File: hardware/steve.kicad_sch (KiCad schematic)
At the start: 10 parts, among them J1 Conn_ARM_JTAG_SWD_10, U1 STM32F407VGTx, Y1 12MHz, Y2 32.768kHz

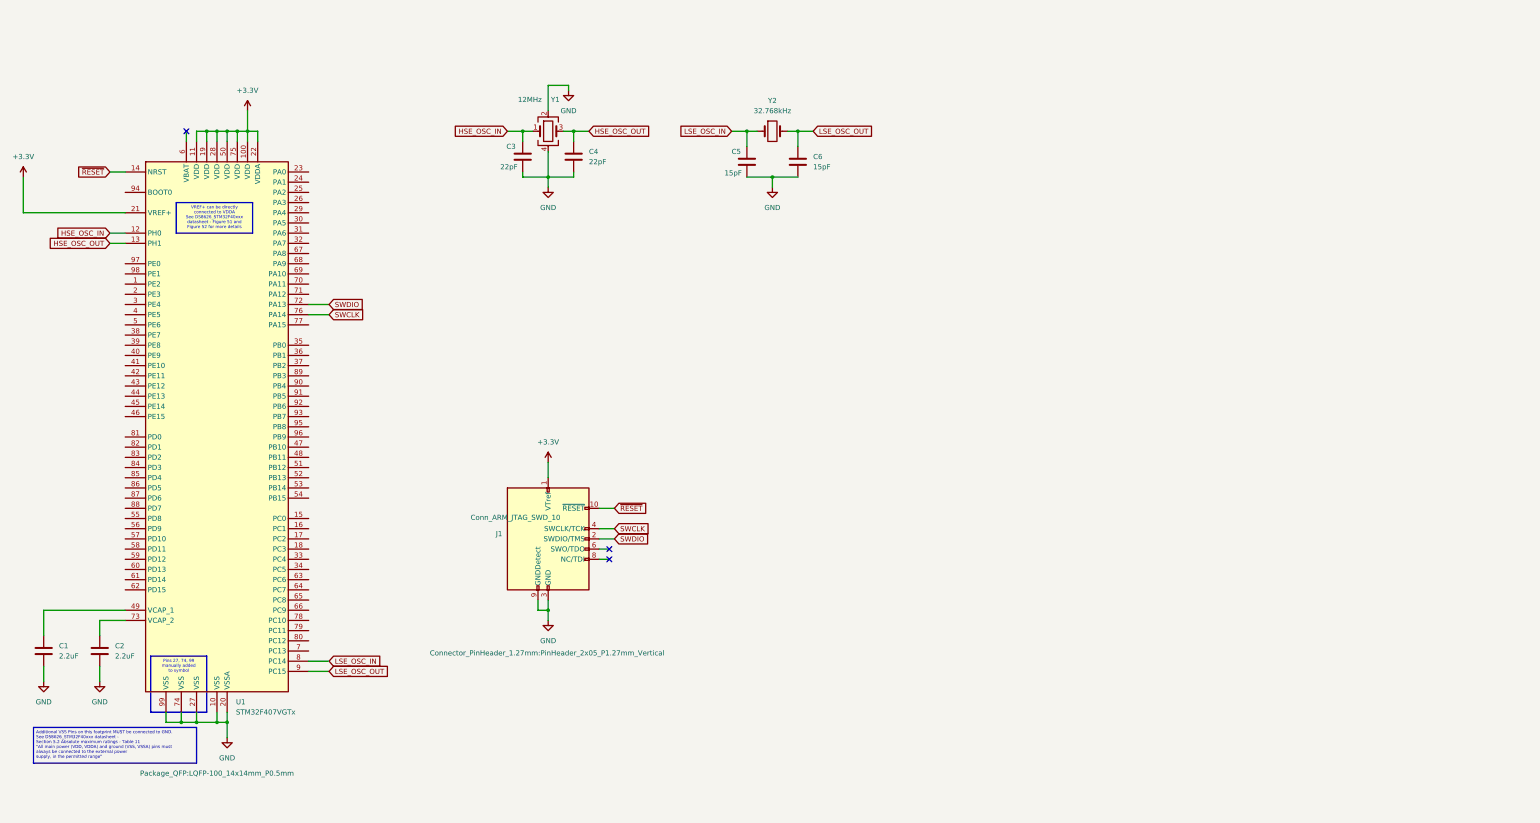
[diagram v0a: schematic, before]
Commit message: Added 5V reg and other components
Added 5V regulator circuit to schematic. Added project libraries for imported symbols and footprints. Added additional components to schematic.
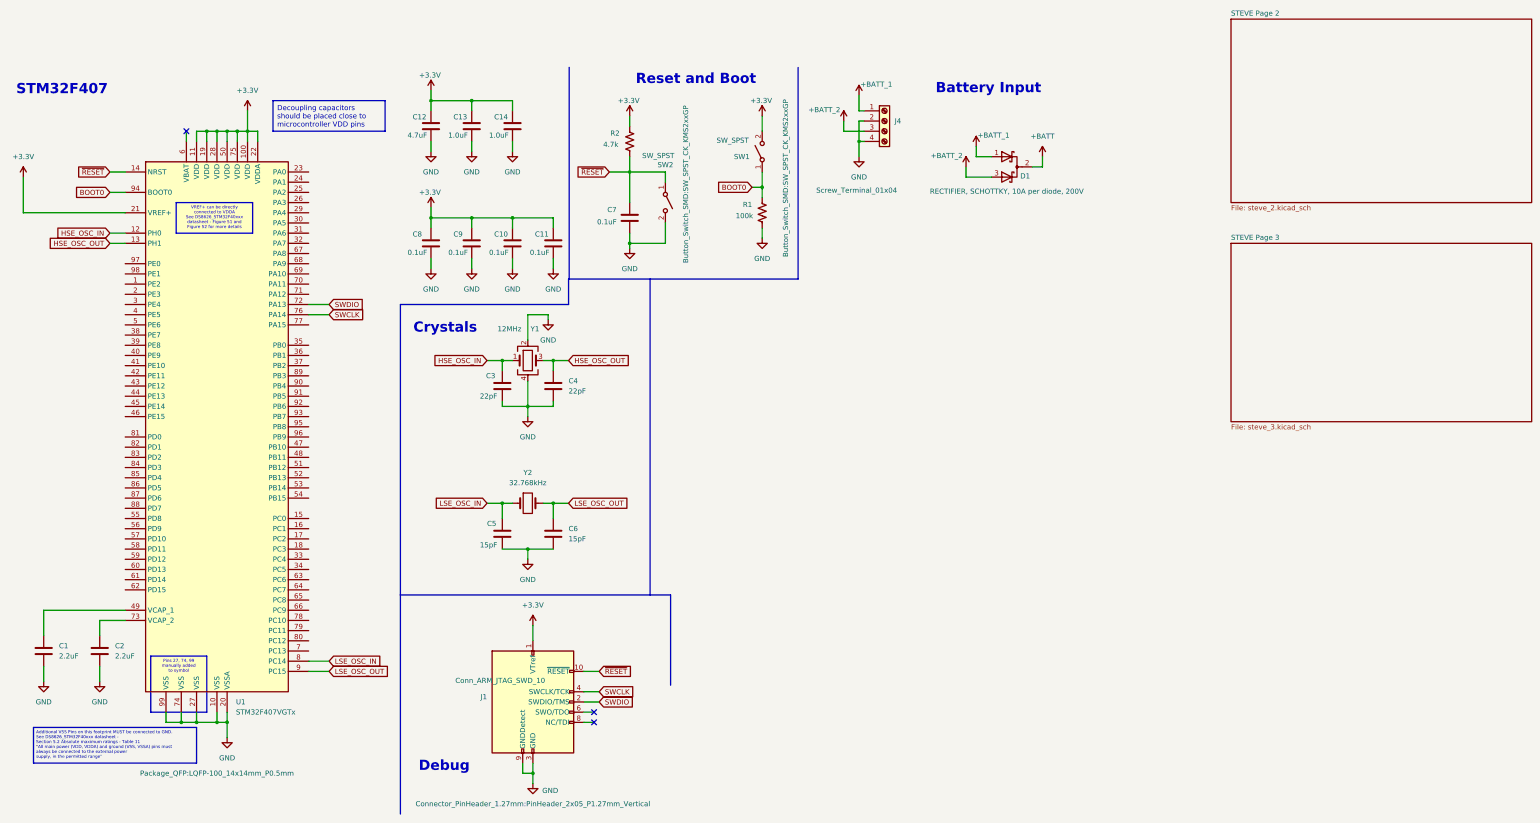
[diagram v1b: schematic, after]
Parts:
- added C10, C11, C7, C8, C9: 0.1uF, Capacitor_SMD:C_0603_1608Metric, symbol Device:C
- added C12: 4.7uF, Capacitor_SMD:C_0603_1608Metric, symbol Device:C
- added C13, C14: 1.0uF, Capacitor_SMD:C_0603_1608Metric, symbol Device:C
- added D1: RECTIFIER, SCHOTTKY, 10A per diode, 200V, Package_TO_SOT_SMD:TO-263-2, symbol Device:D_Schottky_Dual_CommonCathode_AKA_Parallel
- added J4: Screw_Terminal_01x04, TerminalBlock_Phoenix:TerminalBlock_Phoenix_PT-1,5-4-5.0-H_1x04_P5.00mm_Horizontal, symbol Connector:Screw_Terminal_01x04
- added R1: 100k, Resistor_SMD:R_0603_1608Metric, symbol Device:R_US
- added R2: 4.7k, Resistor_SMD:R_0603_1608Metric, symbol Device:R_US
- added SW1, SW2: SW_SPST, Button_Switch_SMD:SW_SPST_CK_KMS2xxGP, symbol Switch:SW_SPST
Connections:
- net +3.3V: now also C10.1, C11.1, C12.1, C13.1, C14.1, C8.1, C9.1, R2.1, SW1.2 (B)
- net GND: now also C10.2, C11.2, C12.2, C13.2, C14.2, C7.2, C8.2, C9.2, J4.2 (Pin_2), J4.4 (Pin_4), R1.2, SW2.2 (B)
- net ~{RESET}: now also C7.1, R2.2, SW2.1 (A)
- net BOOT0: now reaches U1.94 (BOOT0)
- net BOOT0: now also R1.1, SW1.1 (A)
- new net +BATT: D1.2 (K)
- new net +BATT_1: D1.1 (A), J4.1 (Pin_1)
- new net +BATT_2: D1.3 (A), J4.3 (Pin_3)
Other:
- added sheet STEVE Page 2 (steve_2.kicad_sch)
- added sheet STEVE Page 3 (steve_3.kicad_sch)
- note added: "Battery Input"
- note added: "Crystals"
- note added: "Debug"
- note added: "Reset and Boot"
- note added: "STM32F407"
- moved on the sheet: C3, C4, C5, C6, J1, Y1, Y2

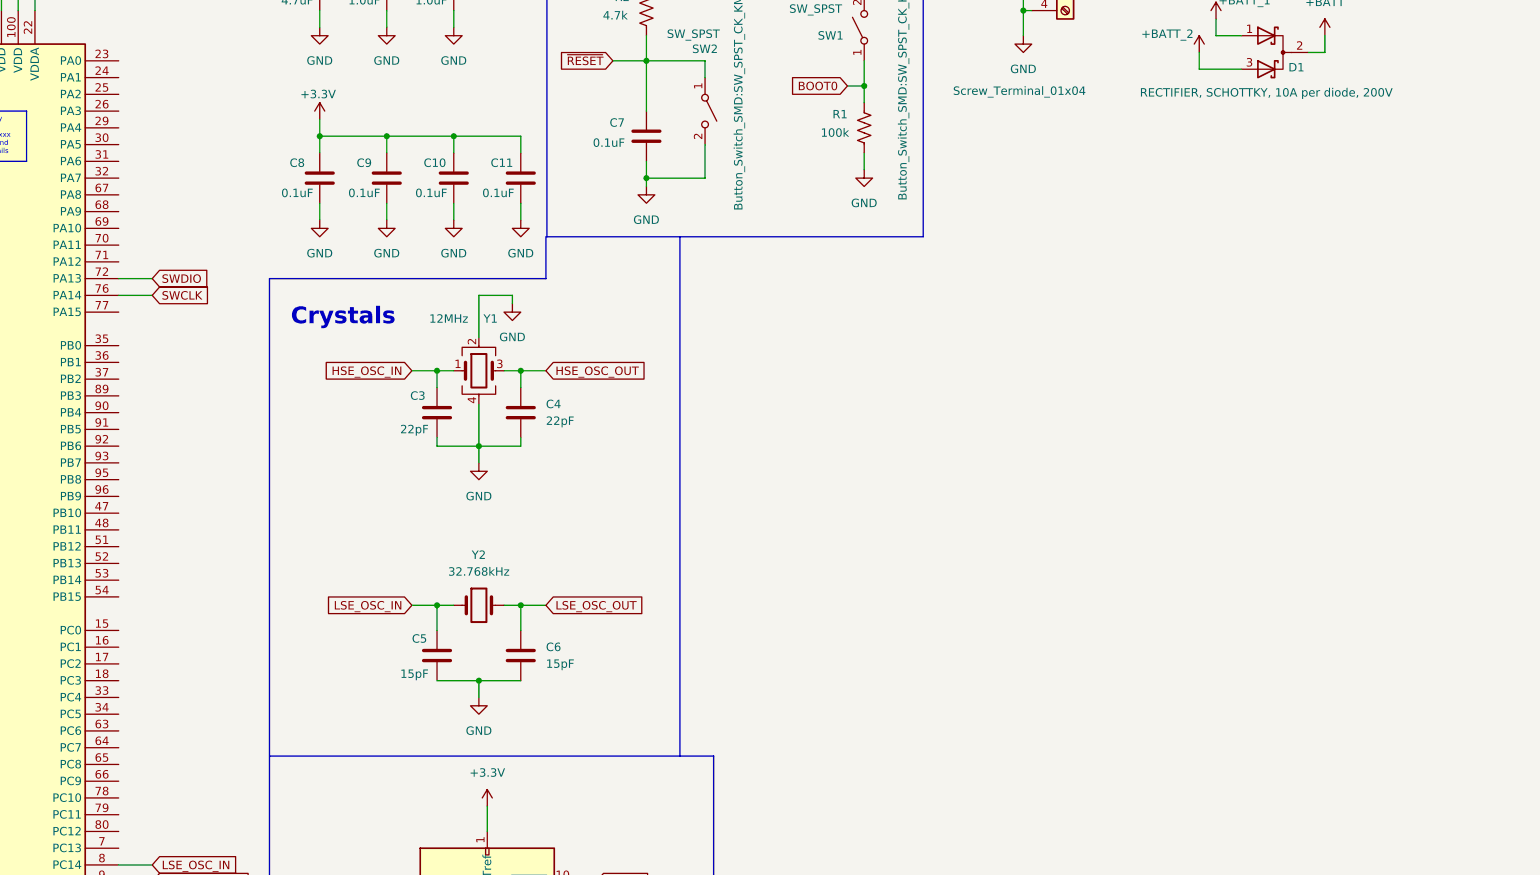
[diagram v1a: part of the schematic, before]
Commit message: import BMP388, add BMP388 to pcb and sch
Import BMP388 symbol and footprint to project imports dir. Add BMP388 symbol to schematic and footprint to pcb.
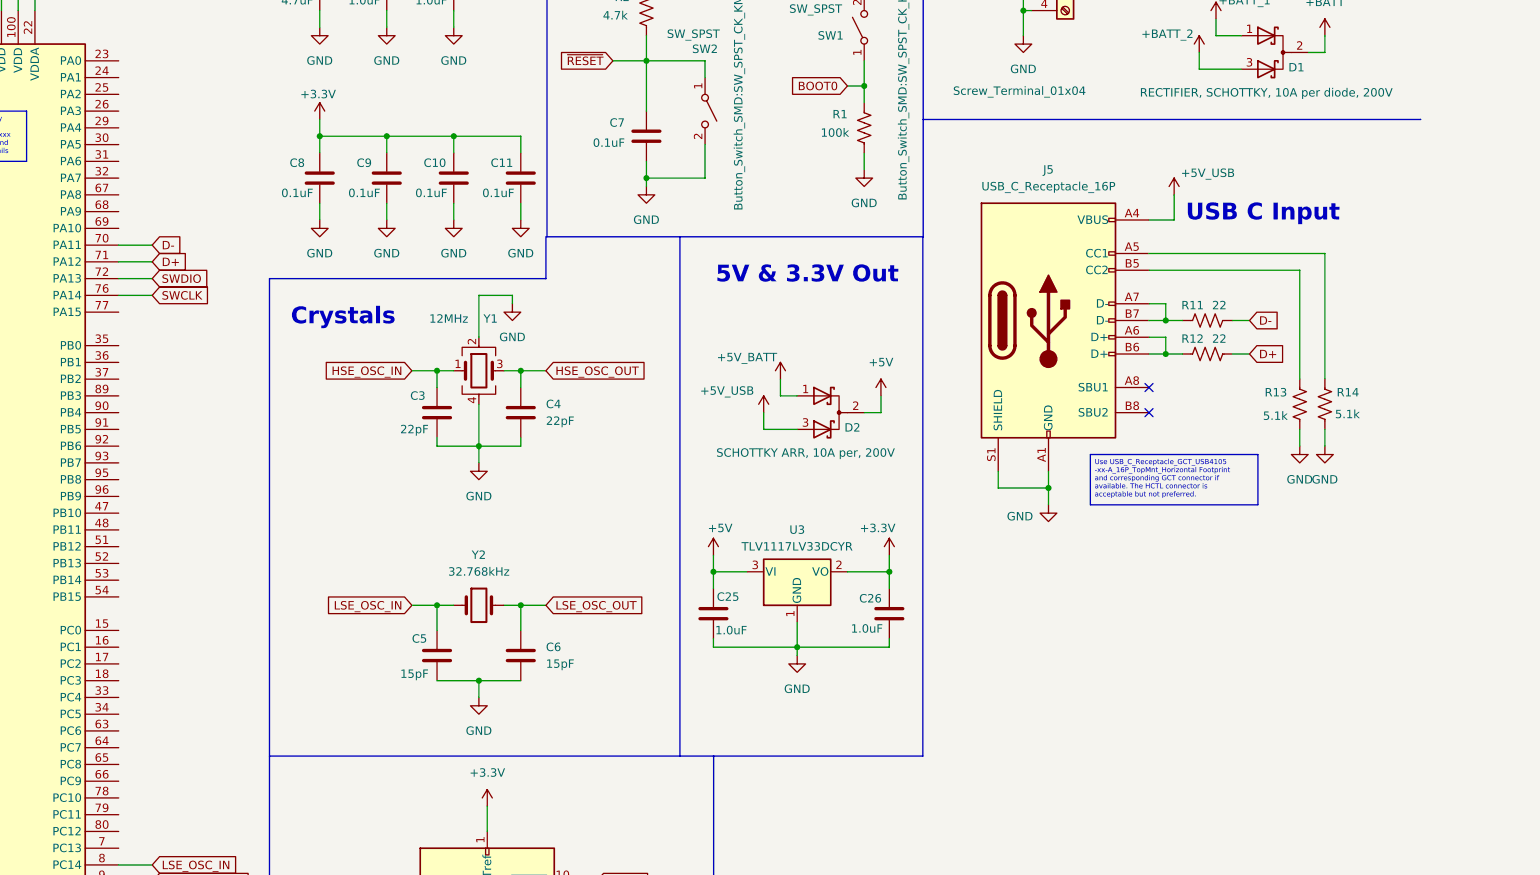
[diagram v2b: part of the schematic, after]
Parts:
- added C25, C26: 1.0uF, Capacitor_SMD:C_1206_3216Metric, symbol Device:C
- added D2: SCHOTTKY ARR, 10A per, 200V, Package_TO_SOT_SMD:TO-263-2, symbol Device:D_Schottky_Dual_CommonCathode_AKA_Parallel
- added J5: USB_C_Receptacle_16P, Connector_USB:USB_C_Receptacle_HCTL_HC-TYPE-C-16P-01A, symbol Connector:USB_C_Receptacle_USB2.0_14P
- added R11, R12: 22, Resistor_SMD:R_0603_1608Metric, symbol Device:R_US
- added R13, R14: 5.1k, Resistor_SMD:R_0603_1608Metric, symbol Device:R_US
- added U3: TLV1117LV33DCYR, Package_TO_SOT_SMD:SOT-223-3_TabPin2, symbol Regulator_Linear:TLV1117-33
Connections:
- net +3.3V: now also C26.1, U3.2 (VO)
- net GND: now also C25.2, C26.2, J5.A1 (GND), J5.A12 (GND), J5.B1 (GND), J5.B12 (GND), J5.S1 (SHIELD), R13.2, R14.2, U3.1 (GND)
- net D-: now reaches U1.70 (PA11)
- net D-: now also R11.2
- net D+: now reaches U1.71 (PA12)
- net D+: now also R12.2
- new net: J5.A5 (CC1), R14.1
- new net: J5.A7 (D-), J5.B7 (D-), R11.1
- new net: J5.A6 (D+), J5.B6 (D+), R12.1
- new net: J5.B5 (CC2), R13.1
- new net +5V: C25.1, D2.2 (K), U3.3 (VI)
- new net +5V_BATT: D2.1 (A)
- new net +5V_USB: D2.3 (A), J5.A4 (VBUS), J5.A9 (VBUS), J5.B4 (VBUS), J5.B9 (VBUS)
- no-connect marks 3 -> 5
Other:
- note added: "5V & 3.3V Out"
- note added: "USB C Input"

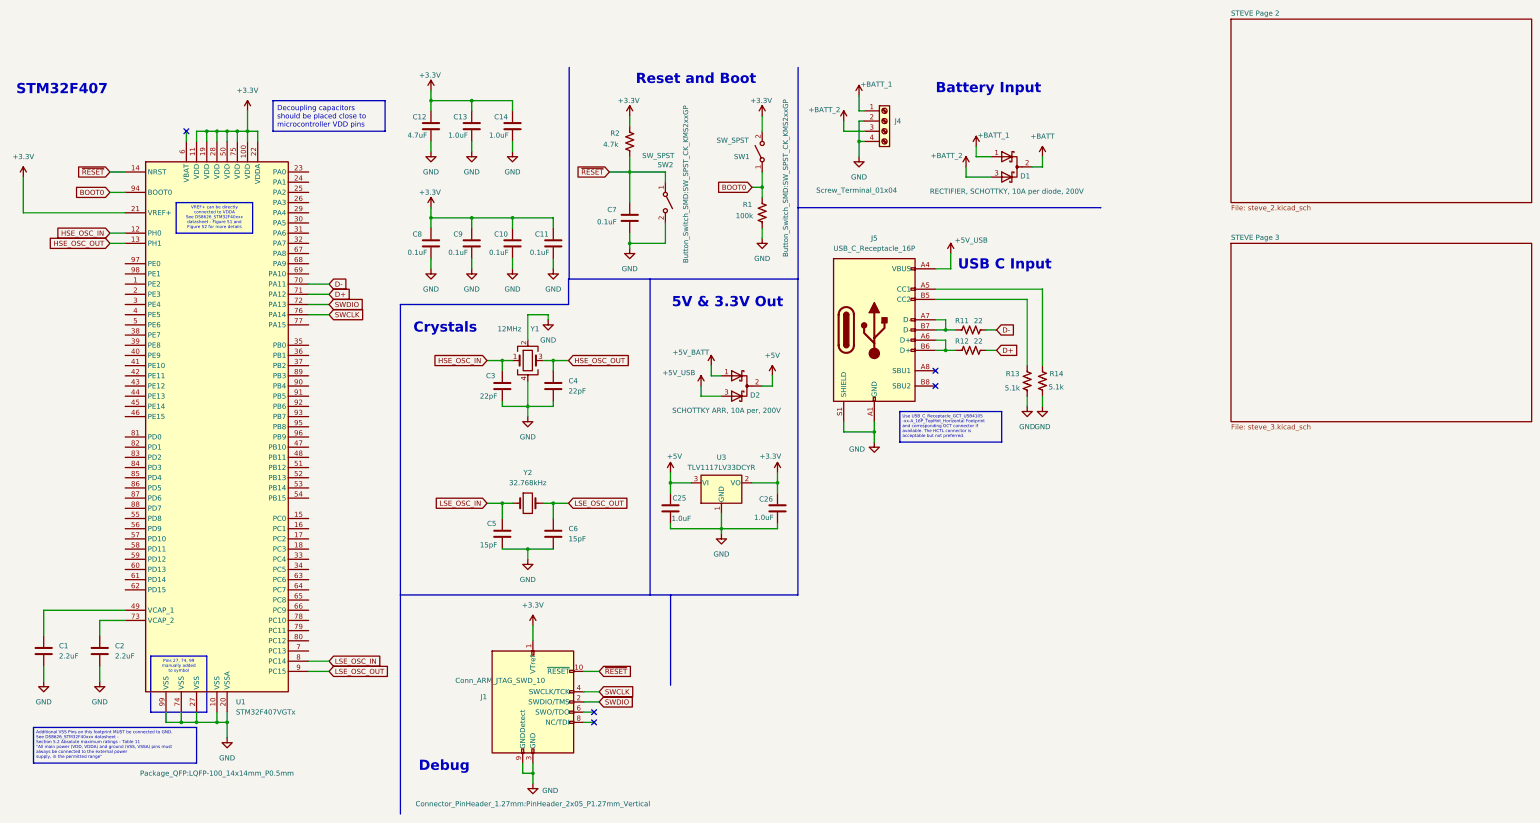
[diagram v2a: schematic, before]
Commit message: Finished sensor, flash, and SD card in schematic; Updated README for remaining items
Finished BMI270 and BMP390, Flash storage, and  microSD card in schematic; Updated README for remaining items
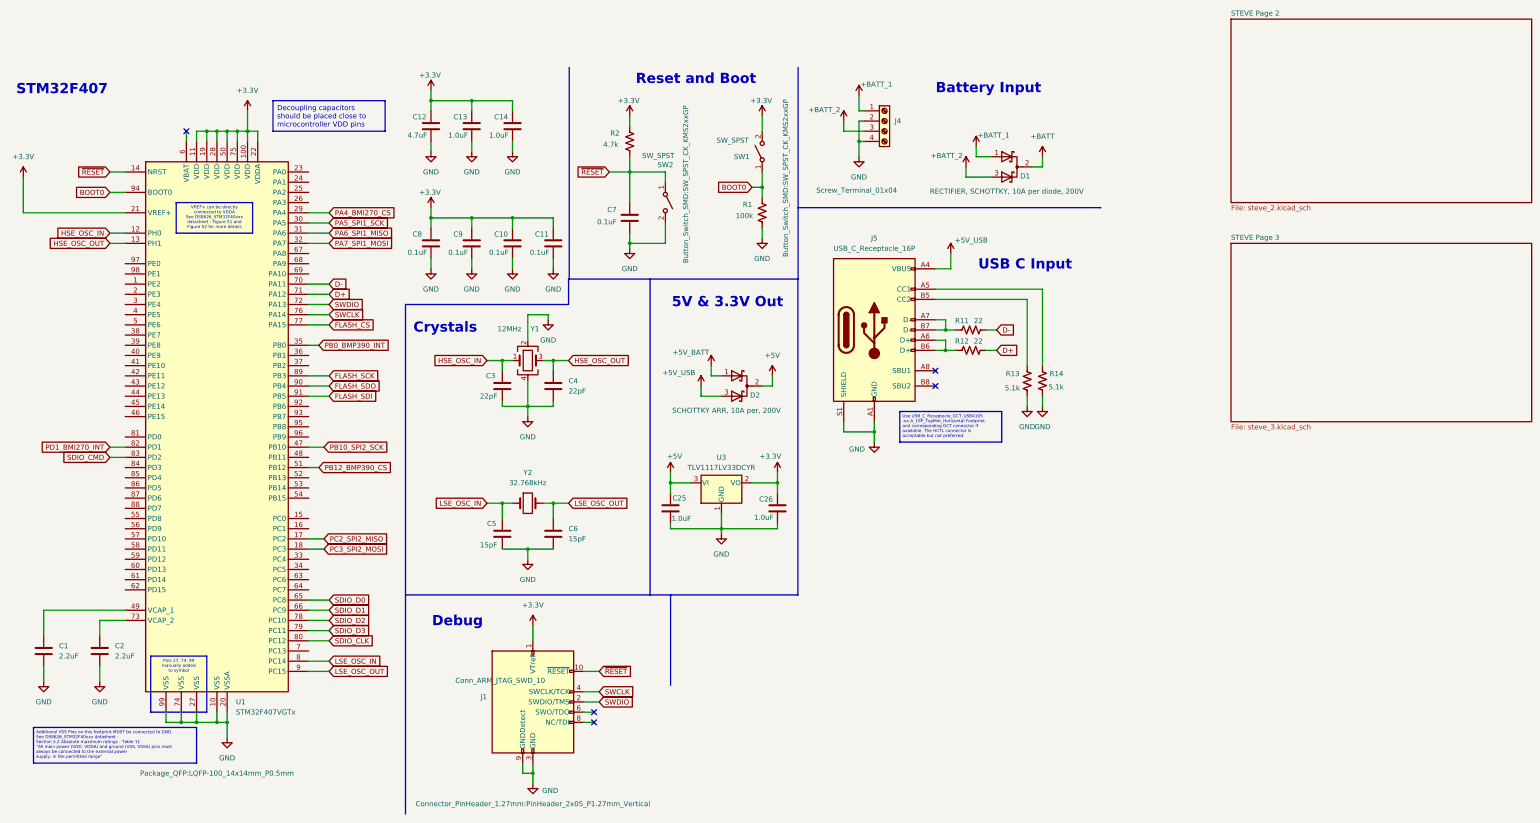
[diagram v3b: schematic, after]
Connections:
- net PC2_SPI2_MISO: now reaches U1.17 (PC2)
- net PC3_SPI2_MOSI: now reaches U1.18 (PC3)
- net PA4_BMI270_CS: now reaches U1.29 (PA4)
- net PA5_SPI1_SCK: now reaches U1.30 (PA5)
- net PA6_SPI1_MISO: now reaches U1.31 (PA6)
- net PA7_SPI1_MOSI: now reaches U1.32 (PA7)
- net PB0_BMP390_INT: now reaches U1.35 (PB0)
- net PB10_SPI2_SCK: now reaches U1.47 (PB10)
- net PB12_BMP390_CS: now reaches U1.51 (PB12)
- net SDIO_D0: now reaches U1.65 (PC8)
- net SDIO_D1: now reaches U1.66 (PC9)
- net FLASH_CS: now reaches U1.77 (PA15)
- net SDIO_D2: now reaches U1.78 (PC10)
- net SDIO_D3: now reaches U1.79 (PC11)
- net SDIO_CLK: now reaches U1.80 (PC12)
- net PD1_BMI270_INT: now reaches U1.82 (PD1)
- net SDIO_CMD: now reaches U1.83 (PD2)
- net FLASH_SCK: now reaches U1.89 (PB3)
- net FLASH_SDO: now reaches U1.90 (PB4)
- net FLASH_SDI: now reaches U1.91 (PB5)
